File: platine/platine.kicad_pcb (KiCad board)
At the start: 2 copper layers, 66 x 40.6 mm, 17 parts, among them J1 Screw_Terminal_01x02, J2 Screw_Terminal_01x02, J3 Screw_Terminal_01x02, Q1 BC547, Q2 BC337, SW1 SW_Push_Dual, U1 ATtiny13A-PU

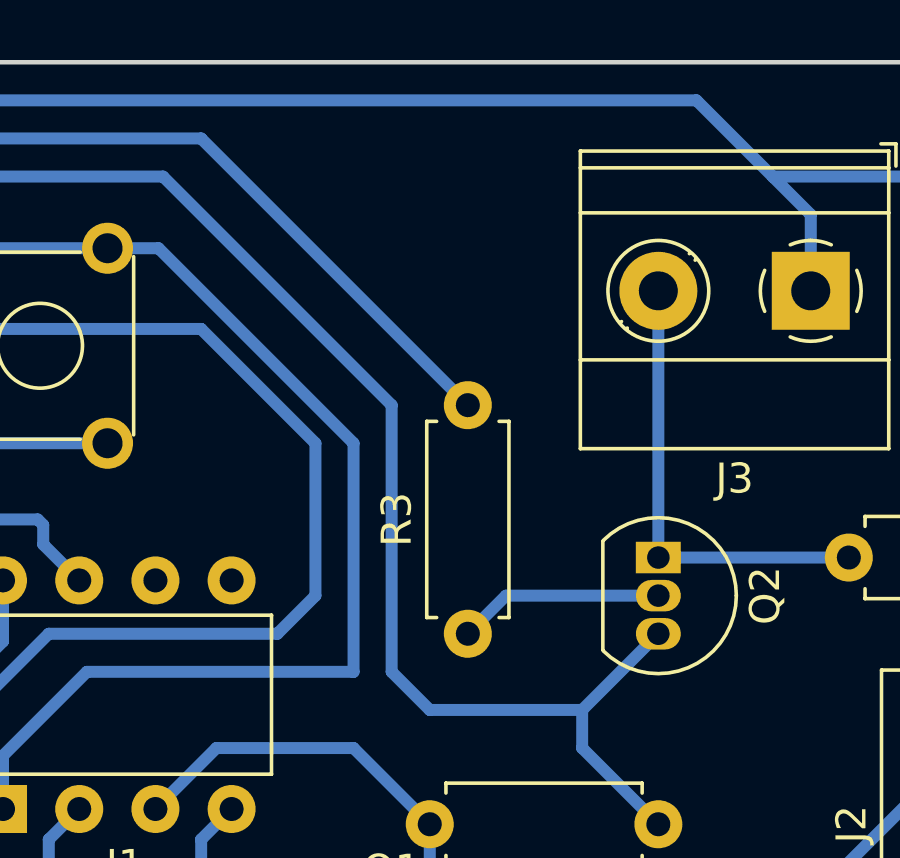
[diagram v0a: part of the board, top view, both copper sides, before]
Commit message: PCB: Added capacitor to smooth signal
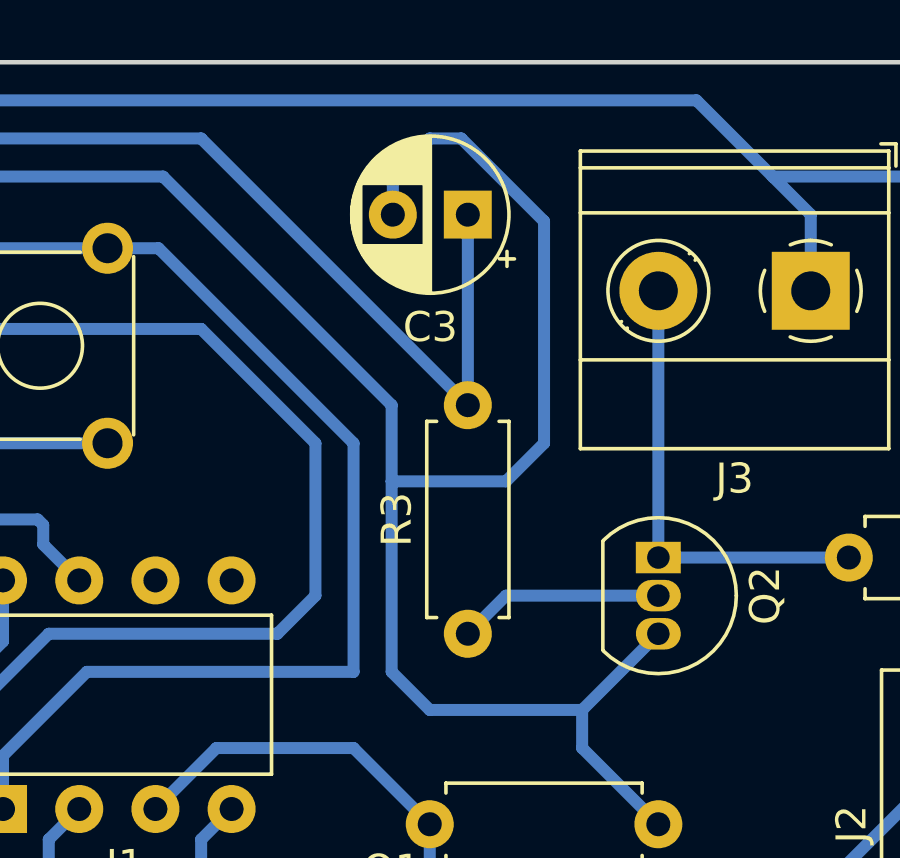
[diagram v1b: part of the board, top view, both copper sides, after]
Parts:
- added C3: 100µ, Capacitor_THT:CP_Radial_D5.0mm_P2.50mm, F.Cu at (102.9, 94.0)
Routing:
- net GND: track 158.4 -> 179.4 mm
- net Pump: track 68.8 -> 75.1 mm
